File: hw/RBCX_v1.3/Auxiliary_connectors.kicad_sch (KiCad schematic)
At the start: 45 parts

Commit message: Remove stepdowns, Micro-USB; fixup region names
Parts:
- removed X4: (no value), symbol RBCX-eagle-import:614105150621
- D12: value (none) -> SS34; footprint (none) -> RBCX:SMA
- JP32: value (none) -> USB; footprint (none) -> RBCX:1X05
- JP33: value (none) -> SWD; footprint (none) -> RBCX:1X06
- JP34: value (none) -> DEBUG; footprint (none) -> RBCX:1X04
- JP35: value (none) -> USBC_AUX; footprint (none) -> RBCX:1X04
- JP36: value (none) -> BOOT_SW; footprint (none) -> RBCX:1X02
- JP37: value (none) -> ESP32_JTAG; footprint (none) -> RBCX:1X06
- JP38: value (none) -> MPU_I2C; footprint (none) -> RBCX:1X04
- JP39: value (none) -> EXPANDER_UART; footprint (none) -> RBCX:1X06
- JP40: value (none) -> ESP_PROG_UART; footprint (none) -> RBCX:1X04
- JP41: value (none) -> EXPANDER_CAN/I2C; footprint (none) -> RBCX:1X06
- Q9: footprint (none) -> RBCX:SOT23
- R66, R68, R69, R72, R73, R74, R80, R81, R82, R83, R84, R85, R86, R87, R88, R89: value (none) -> 330R; footprint (none) -> RBCX:R0402
- R67: footprint (none) -> RBCX:R0402
- R70: value (none) -> 5k6; footprint (none) -> RBCX:R0402
- R71: value (none) -> 10k; footprint (none) -> RBCX:R0402
- R75: value (none) -> 100k; footprint (none) -> RBCX:R0402
- R76, R77: value (none) -> 5k1; footprint (none) -> RBCX:R0402
- R78, R79: value (none) -> 4k7; footprint (none) -> RBCX:R0402
- SJ6, SJ7: value (none) -> SJ2W0603; footprint (none) -> RBCX:SJ_2_0603
- TP17, TP18, TP19, TP20: value (none) -> TP_06MM; footprint (none) -> RBCX:TP_06
- X3: value (none) -> 52559-3092; footprint (none) -> RBCX:52559-3092
- X5: value (none) -> USB_C_8PIN; footprint (none) -> RBCX:USB_C_VERT_THT_8PIN
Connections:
- net USB_ID: no longer names the net of JP32.4

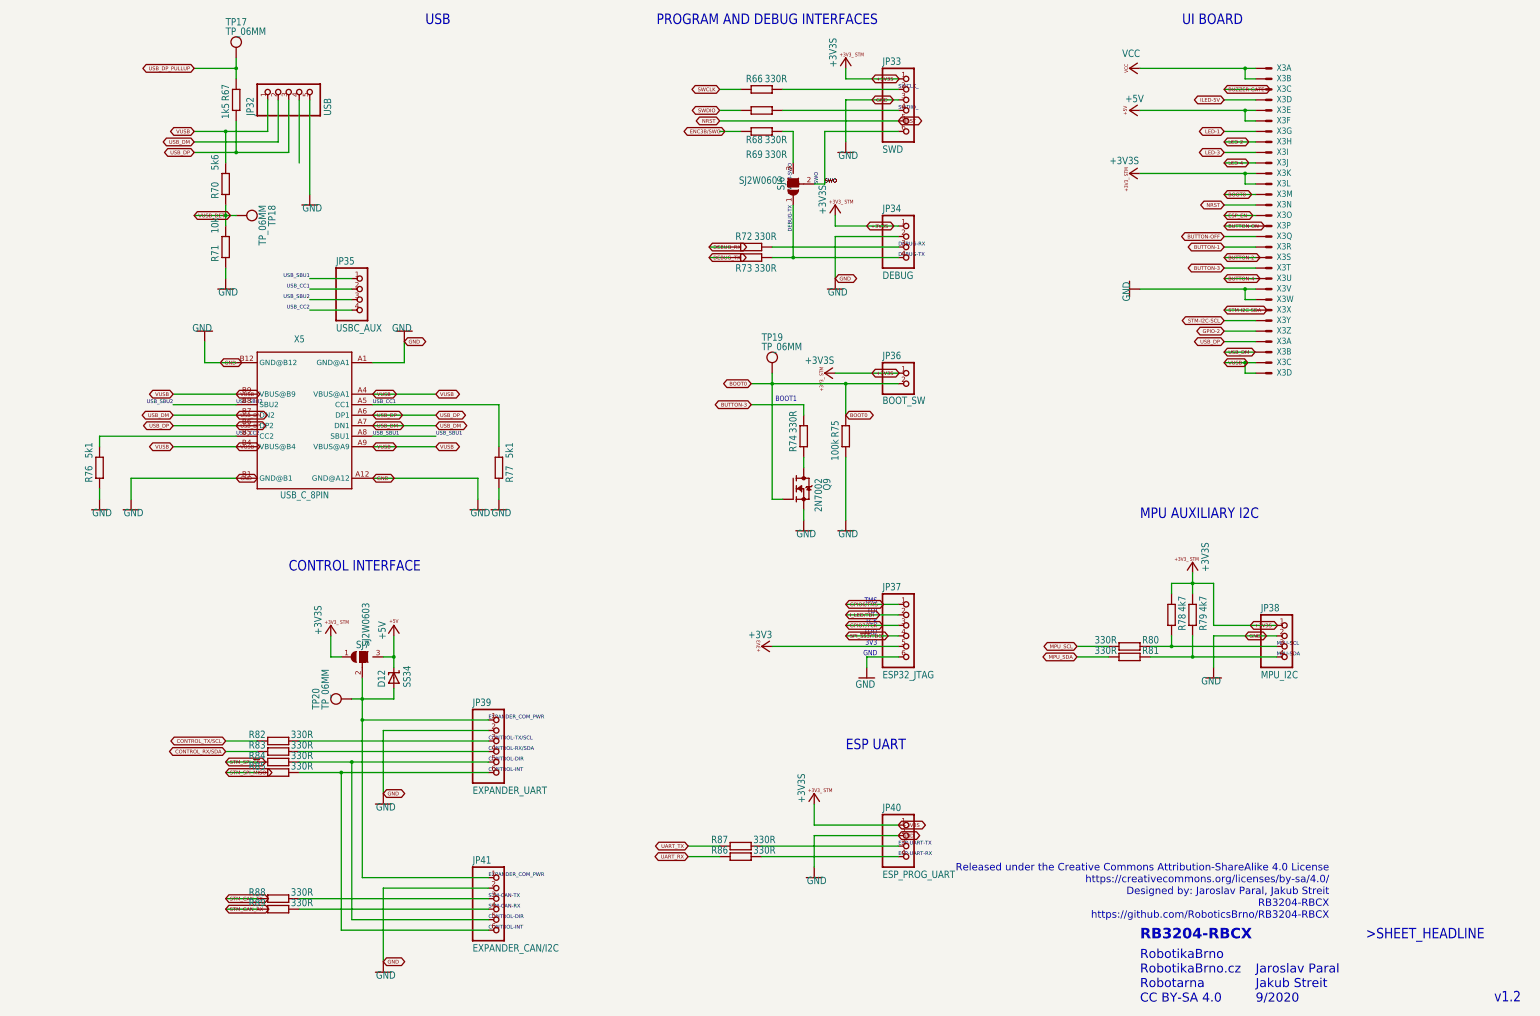
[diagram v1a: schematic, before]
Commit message: Everything everywhere all et once
Conversion to a new look
-  splitting the whole diagram for better orientation on multiple sheets using Kicad functions. Division of the whole schematics within several hierarchical sheets without globally named trac, using only wires, local labels and hierarchical labels.

Add new features
- Battery charger with cell balancer (With whole battery measurement)
- USB PD Sink Controller

Change old features
-  removing many 5V stepdowns and replacing them with only one strong stepdown (continuous 8A, peak 12A)
-  New power switcher design to connect VUSB to the VCC power line when no battery is connected.
(The reason for the new design is the implementation of Power deliveri => high voltage capability on VUSB 5-12V).

Remove micro_USB
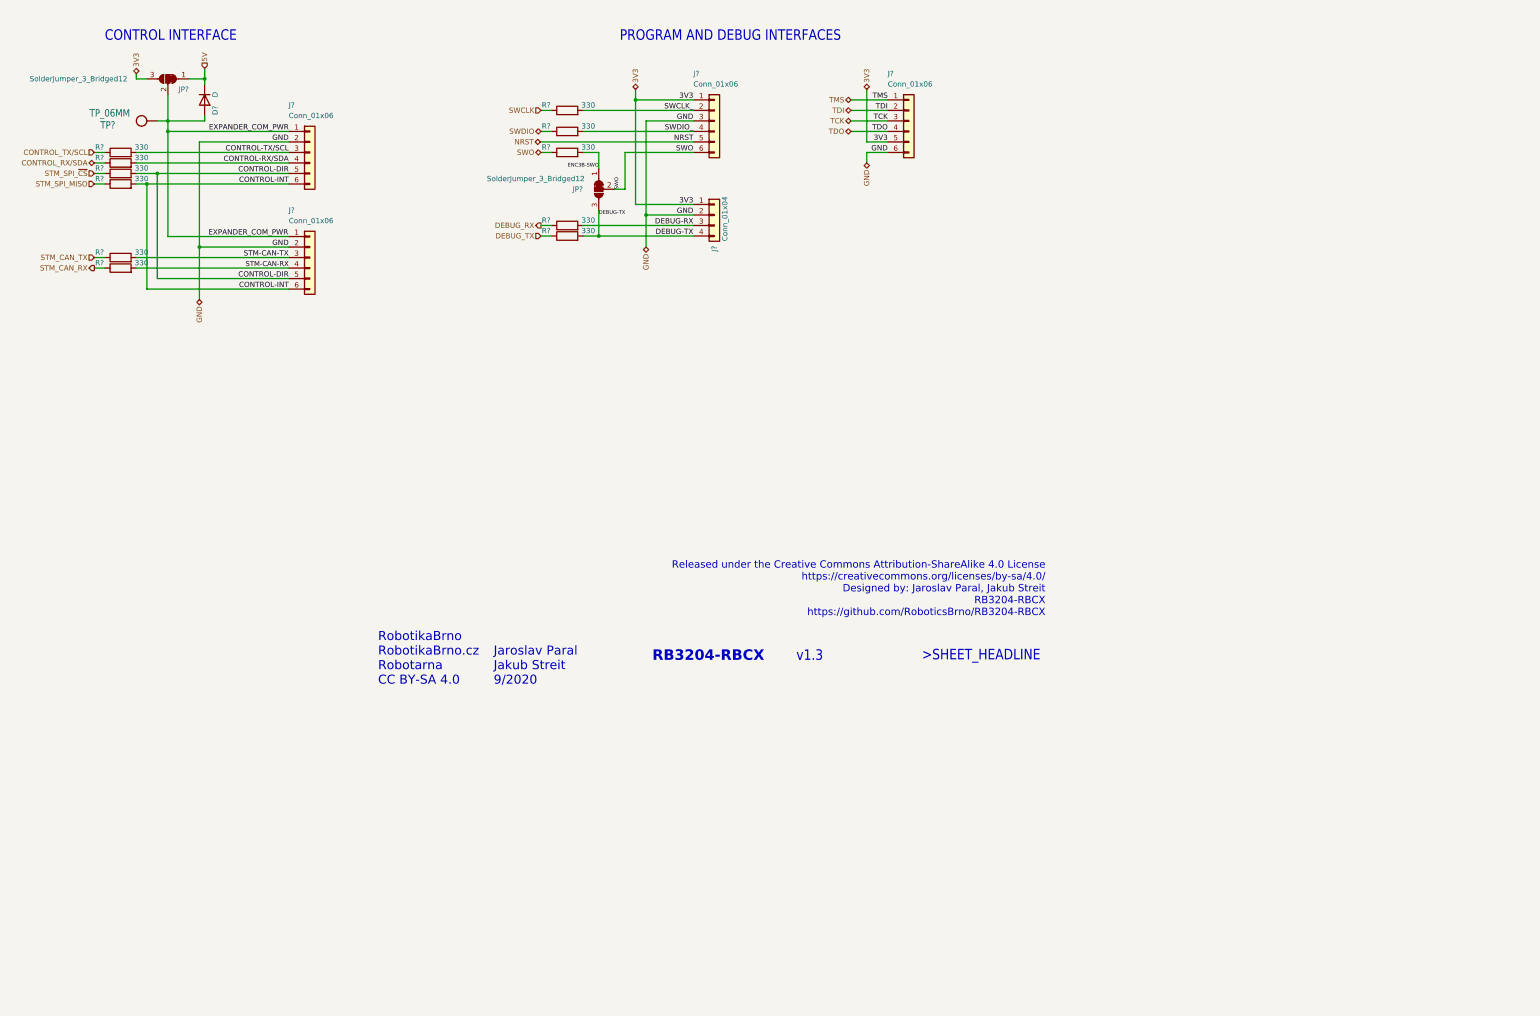
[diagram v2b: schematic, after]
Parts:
- removed D12: SS34, RBCX:SMA, symbol RBCX-eagle-import:SHOTTKY-SMA
- removed JP32: USB, RBCX:1X05, symbol RBCX-eagle-import:PINHD-1X5
- removed JP33: SWD, RBCX:1X06, symbol RBCX-eagle-import:PINHD-1X6
- removed JP34: DEBUG, RBCX:1X04, symbol RBCX-eagle-import:PINHD-1X4
- removed JP35: USBC_AUX, RBCX:1X04, symbol RBCX-eagle-import:PINHD-1X4
- removed JP36: BOOT_SW, RBCX:1X02, symbol RBCX-eagle-import:PINHD-1X2
- removed JP37: ESP32_JTAG, RBCX:1X06, symbol RBCX-eagle-import:PINHD-1X6
- removed JP38: MPU_I2C, RBCX:1X04, symbol RBCX-eagle-import:PINHD-1X4
- removed JP39: EXPANDER_UART, RBCX:1X06, symbol RBCX-eagle-import:PINHD-1X6
- removed JP40: ESP_PROG_UART, RBCX:1X04, symbol RBCX-eagle-import:PINHD-1X4
- removed JP41: EXPANDER_CAN/I2C, RBCX:1X06, symbol RBCX-eagle-import:PINHD-1X6
- removed Q9: (no value), RBCX:SOT23, symbol RBCX-eagle-import:N-MOSFET-SOT23-GSD
- removed R66, R68, R69, R72, R73, R74, R80, R81, R82, R83, R84, R85, R86, R87, R88, R89: 330R, RBCX:R0402, symbol RBCX-eagle-import:R-EU_R0402
- removed R67: (no value), RBCX:R0402, symbol RBCX-eagle-import:R-EU_R0402
- removed R70: 5k6, RBCX:R0402, symbol RBCX-eagle-import:R-EU_R0402
- removed R71: 10k, RBCX:R0402, symbol RBCX-eagle-import:R-EU_R0402
- removed R75: 100k, RBCX:R0402, symbol RBCX-eagle-import:R-EU_R0402
- removed R76, R77: 5k1, RBCX:R0402, symbol RBCX-eagle-import:R-EU_R0402
- removed R78, R79: 4k7, RBCX:R0402, symbol RBCX-eagle-import:R-EU_R0402
- removed SJ6, SJ7: SJ2W0603, RBCX:SJ_2_0603, symbol RBCX-eagle-import:SJ2W0603
- removed TP17, TP18, TP19, TP20: TP_06MM, RBCX:TP_06, symbol RBCX-eagle-import:TP_06MM
- removed X3: 52559-3092, RBCX:52559-3092, symbol RBCX-eagle-import:52559-3092
- removed X5: USB_C_8PIN, RBCX:USB_C_VERT_THT_8PIN, symbol RBCX-eagle-import:USB_C_8PIN
- added D?: D, Diode_SMD:D_SOD-523, symbol Device:D
- added J? (x4): Conn_01x06, Connector_PinHeader_2.54mm:PinHeader_1x06_P2.54mm_Vertical, symbol Connector_Generic:Conn_01x06
- added J?: Conn_01x04, Connector_PinHeader_2.54mm:PinHeader_1x04_P2.54mm_Vertical, symbol Connector_Generic:Conn_01x04
- added JP? (x2): SolderJumper_3_Bridged12, Jumper:SolderJumper-3_P1.3mm_Bridged12_RoundedPad1.0x1.5mm, symbol Jumper:SolderJumper_3_Bridged12
- added R? (x11): 330, Capacitor_SMD:C_0201_0603Metric, symbol Device:R
- added TP?: TP_06MM, RBCX:TP_06MM, symbol RBCX-eagle-import:TP_06MM
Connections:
- net CONTROL-DIR: now also J?.5 (Pin_5), J?.5 (Pin_5), R?.2
- net CONTROL-INT: now also J?.6 (Pin_6), J?.6 (Pin_6), R?.2
- net DEBUG-RX: now also J?.3 (Pin_3), R?.2
- net DEBUG-TX: now also J?.4 (Pin_4), JP?.3 (B), R?.2
- net DEBUG_RX: now also R?.1
- net DEBUG_TX: now also R?.1
- net ENC3B-SWO: now also JP?.1 (A), R?.2
- net EXPANDER_COM_PWR: now also D?.2 (A), J?.1 (Pin_1), J?.1 (Pin_1), JP?.2 (C), TP?.P$1 (TP)
- net GND: now also J?.2 (Pin_2), J?.2 (Pin_2), J?.2 (Pin_2), J?.3 (Pin_3), J?.6 (Pin_6)
- net NRST: now also J?.5 (Pin_5)
- net STM-CAN-RX: now also J?.4 (Pin_4), R?.2
- net STM-CAN-TX: now also J?.3 (Pin_3), R?.2
- net STM_CAN_RX: now also R?.1
- net STM_CAN_TX: now also R?.1
- net STM_SPI_MISO: now also R?.1
- net STM_SPI_~{CS}: now also R?.1
- net SWCLK: now also R?.1
- net SWCLK_: now also J?.2 (Pin_2), R?.2
- net SWDIO: now also R?.1
- net SWDIO_: now also J?.4 (Pin_4), R?.2
- net SWO: now also J?.6 (Pin_6), JP?.2 (C), R?.1
- new net 3V3: J?.1 (Pin_1), J?.1 (Pin_1), J?.5 (Pin_5), JP?.3 (B)
- new net 5V: D?.1 (K), JP?.1 (A)
- new net CONTROL-RX/SDA: J?.4 (Pin_4), R?.2
- new net CONTROL-TX/SCL: J?.3 (Pin_3), R?.2
- new net CONTROL_RX/SDA: R?.1
- new net CONTROL_TX/SCL: R?.1
- new net TCK: J?.3 (Pin_3)
- new net TDI: J?.2 (Pin_2)
- new net TDO: J?.4 (Pin_4)
- new net TMS: J?.1 (Pin_1)
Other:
- note added: "v1.3"
- note removed: "3V3"
- note removed: "BOOT1"
- note removed: "ESP UART"
- note removed: "GND"
- note removed: "MPU AUXILIARY I2C"
- note removed: "TCK"
- note removed: "TDI"
- note removed: "TDO"
- note removed: "TMS"
- note removed: "UI BOARD"
- note removed: "USB"
- note removed: "v1.2"

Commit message: Work in progress
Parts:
- gave numbers to parts that had none: 20
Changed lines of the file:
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@@
   (symbol (lib_id "Device:R") (at 60.96 73.66 90) (unit 1)
     (in_bom yes) (on_board yes)
-    (property "Reference" "R?" (id 0) (at 55.88 72.39 90))
+    (property "Reference" "R50" (id 0) (at 55.88 72.39 90))
     (property "Value" "330" (id 1) (at 66.04 72.39 90))
     (property "Footprint" "Capacitor_SMD:C_0201_0603Metric" (id 2) (at 60.96 75.438 90)
@@
   (symbol (lib_id "Device:R") (at 60.96 93.98 90) (unit 1)
     (in_bom yes) (on_board yes)
-    (property "Reference" "R?" (id 0) (at 55.88 92.71 90))
+    (property "Reference" "R54" (id 0) (at 55.88 92.71 90))
     (property "Value" "330" (id 1) (at 66.04 92.71 90))
     (property "Footprint" "Capacitor_SMD:C_0201_0603Metric" (id 2) (at 60.96 95.758 90)
@@
   (symbol (lib_id "Device:R") (at 168.91 58.42 90) (unit 1)
     (in_bom yes) (on_board yes)
-    (property "Reference" "R?" (id 0) (at 163.83 57.15 90))
+    (property "Reference" "R45" (id 0) (at 163.83 57.15 90))
     (property "Value" "330" (id 1) (at 173.99 57.15 90))
     (property "Footprint" "Capacitor_SMD:C_0201_0603Metric" (id 2) (at 168.91 60.198 90)
@@
   (symbol (lib_id "Device:R") (at 60.96 71.12 90) (unit 1)
     (in_bom yes) (on_board yes)
-    (property "Reference" "R?" (id 0) (at 55.88 69.85 90))
+    (property "Reference" "R49" (id 0) (at 55.88 69.85 90))
     (property "Value" "330" (id 1) (at 66.04 69.85 90))
     (property "Footprint" "Capacitor_SMD:C_0201_0603Metric" (id 2) (at 60.96 72.898 90)
@@
   (symbol (lib_id "Connector_Generic:Conn_01x06") (at 106.68 68.58 0) (unit 1)
     (in_bom yes) (on_board yes)
-    (property "Reference" "J?" (id 0) (at 101.6 57.15 0)
+    (property "Reference" "J26" (id 0) (at 101.6 57.15 0)
       (effects (font (size 1.27 1.27)) (justify left))
     )
@@
   (symbol (lib_id "Jumper:SolderJumper_3_Bridged12") (at 176.53 77.47 90) (mirror x) (unit 1)
     (in_bom yes) (on_board yes)
-    (property "Reference" "JP?" (id 0) (at 171.45 77.47 90))
+    (property "Reference" "JP6" (id 0) (at 171.45 77.47 90))
     (property "Value" "SolderJumper_3_Bridged12" (id 1) (at 161.29 74.93 90))
     (property "Footprint" "Jumper:SolderJumper-3_P1.3mm_Bridged12_RoundedPad1.0x1.5mm" (id 2) (at 176.53 77.47 0)
@@
   (symbol (lib_id "Device:R") (at 168.91 63.5 90) (unit 1)
     (in_bom yes) (on_board yes)
-    (property "Reference" "R?" (id 0) (at 163.83 62.23 90))
+    (property "Reference" "R46" (id 0) (at 163.83 62.23 90))
     (property "Value" "330" (id 1) (at 173.99 62.23 90))
     (property "Footprint" "Capacitor_SMD:C_0201_0603Metric" (id 2) (at 168.91 65.278 90)
@@
   (symbol (lib_id "Connector_Generic:Conn_01x06") (at 106.68 93.98 0) (unit 1)
     (in_bom yes) (on_board yes)
-    (property "Reference" "J?" (id 0) (at 101.6 82.55 0)
+    (property "Reference" "J28" (id 0) (at 101.6 82.55 0)
       (effects (font (size 1.27 1.27)) (justify left))
     )
@@
   (symbol (lib_id "Device:R") (at 168.91 86.233 90) (unit 1)
     (in_bom yes) (on_board yes)
-    (property "Reference" "R?" (id 0) (at 163.83 84.963 90))
+    (property "Reference" "R52" (id 0) (at 163.83 84.963 90))
     (property "Value" "330" (id 1) (at 173.99 84.963 90))
     (property "Footprint" "Capacitor_SMD:C_0201_0603Metric" (id 2) (at 168.91 88.011 90)
@@
   (symbol (lib_id "Connector_Generic:Conn_01x04") (at 204.47 83.693 0) (unit 1)
     (in_bom yes) (on_board yes)
-    (property "Reference" "J?" (id 0) (at 204.47 92.583 90)
+    (property "Reference" "J27" (id 0) (at 204.47 92.583 90)
       (effects (font (size 1.27 1.27)) (justify left))
     )
@@
   (symbol (lib_id "RBCX-eagle-import:TP_06MM") (at 69.85 60.96 90) (unit 1)
     (in_bom yes) (on_board yes)
-    (property "Reference" "TP?" (id 0) (at 59.69 60.96 90)
+    (property "Reference" "TP10" (id 0) (at 59.69 60.96 90)
       (effects (font (size 1.778 1.5113)) (justify left bottom))
     )
@@
   (symbol (lib_id "Device:R") (at 60.96 68.58 90) (unit 1)
     (in_bom yes) (on_board yes)
-    (property "Reference" "R?" (id 0) (at 55.88 67.31 90))
+    (property "Reference" "R47" (id 0) (at 55.88 67.31 90))
     (property "Value" "330" (id 1) (at 66.04 67.31 90))
     (property "Footprint" "Capacitor_SMD:C_0201_0603Metric" (id 2) (at 60.96 70.358 90)
@@
   (symbol (lib_id "Connector_Generic:Conn_01x06") (at 204.47 60.96 0) (unit 1)
     (in_bom yes) (on_board yes)
-    (property "Reference" "J?" (id 0) (at 199.39 49.53 0)
+    (property "Reference" "J24" (id 0) (at 199.39 49.53 0)
       (effects (font (size 1.27 1.27)) (justify left))
     )
@@
   (symbol (lib_id "Device:D") (at 81.28 55.88 270) (unit 1)
     (in_bom yes) (on_board yes)
-    (property "Reference" "D?" (id 0) (at 83.82 58.42 0))
+    (property "Reference" "D2" (id 0) (at 83.82 58.42 0))
     (property "Value" "D" (id 1) (at 83.82 54.61 0))
     (property "Footprint" "Diode_SMD:D_SOD-523" (id 2) (at 81.28 55.88 0)
@@
   (symbol (lib_id "Device:R") (at 60.96 96.52 90) (unit 1)
     (in_bom yes) (on_board yes)
-    (property "Reference" "R?" (id 0) (at 55.88 95.25 90))
+    (property "Reference" "R55" (id 0) (at 55.88 95.25 90))
     (property "Value" "330" (id 1) (at 66.04 95.25 90))
     (property "Footprint" "Capacitor_SMD:C_0201_0603Metric" (id 2) (at 60.96 98.298 90)
@@
   (symbol (lib_id "Device:R") (at 60.96 76.2 90) (unit 1)
     (in_bom yes) (on_board yes)
-    (property "Reference" "R?" (id 0) (at 55.88 74.93 90))
+    (property "Reference" "R51" (id 0) (at 55.88 74.93 90))
     (property "Value" "330" (id 1) (at 66.04 74.93 90))
     (property "Footprint" "Capacitor_SMD:C_0201_0603Metric" (id 2) (at 60.96 77.978 90)
@@
   (symbol (lib_id "Device:R") (at 168.91 88.773 90) (unit 1)
     (in_bom yes) (on_board yes)
-    (property "Reference" "R?" (id 0) (at 163.83 87.503 90))
+    (property "Reference" "R53" (id 0) (at 163.83 87.503 90))
     (property "Value" "330" (id 1) (at 173.99 87.503 90))
     (property "Footprint" "Capacitor_SMD:C_0201_0603Metric" (id 2) (at 168.91 90.551 90)
@@
   (symbol (lib_id "Device:R") (at 168.91 68.58 90) (unit 1)
     (in_bom yes) (on_board yes)
-    (property "Reference" "R?" (id 0) (at 163.83 67.31 90))
+    (property "Reference" "R48" (id 0) (at 163.83 67.31 90))
     (property "Value" "330" (id 1) (at 173.99 67.31 90))
     (property "Footprint" "Capacitor_SMD:C_0201_0603Metric" (id 2) (at 168.91 70.358 90)
@@
   (symbol (lib_id "Jumper:SolderJumper_3_Bridged12") (at 72.39 50.8 0) (mirror y) (unit 1)
     (in_bom yes) (on_board yes)
-    (property "Reference" "JP?" (id 0) (at 76.2 53.34 0))
+    (property "Reference" "JP5" (id 0) (at 76.2 53.34 0))
     (property "Value" "SolderJumper_3_Bridged12" (id 1) (at 50.8 50.8 0))
     (property "Footprint" "Jumper:SolderJumper-3_P1.3mm_Bridged12_RoundedPad1.0x1.5mm" (id 2) (at 72.39 50.8 0)
@@
   (symbol (lib_id "Connector_Generic:Conn_01x06") (at 251.46 60.96 0) (unit 1)
     (in_bom yes) (on_board yes)
-    (property "Reference" "J?" (id 0) (at 246.38 49.53 0)
-      (effects (font (size 1.27 1.27)) (justify left))
-    )
+    (property "Reference" "J25" (id 0) (at 246.38 49.53 0)
+      (effects (font (size 1.27 1.27)) (justify left))
+    )

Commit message: New PCB layout
some changes of schema:
- change PD sink AO33772 to AO33771
- remove power switch
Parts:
- J24, J25, J26, J28: footprint Connector_PinHeader_2.54mm:PinHeader_1x06_P2.54mm_Vertical -> RBCX:PinHeader_1x06_P2.54mm_Vertical
- J27: footprint Connector_PinHeader_2.54mm:PinHeader_1x04_P2.54mm_Vertical -> RBCX:PinHeader_1x04_P2.54mm_Vertical
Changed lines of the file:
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@@
       (effects (font (size 1.27 1.27)) (justify left))
     )
-    (property "Footprint" "Connector_PinHeader_2.54mm:PinHeader_1x06_P2.54mm_Vertical" (id 2) (at 106.68 68.58 0)
+    (property "Footprint" "RBCX:PinHeader_1x06_P2.54mm_Vertical" (id 2) (at 106.68 68.58 0)
       (effects (font (size 1.27 1.27)) hide)
     )
@@
       (effects (font (size 1.27 1.27)) (justify left))
     )
-    (property "Footprint" "Connector_PinHeader_2.54mm:PinHeader_1x06_P2.54mm_Vertical" (id 2) (at 106.68 93.98 0)
+    (property "Footprint" "RBCX:PinHeader_1x06_P2.54mm_Vertical" (id 2) (at 106.68 93.98 0)
       (effects (font (size 1.27 1.27)) hide)
     )
@@
       (effects (font (size 1.27 1.27)) (justify left))
     )
-    (property "Footprint" "Connector_PinHeader_2.54mm:PinHeader_1x04_P2.54mm_Vertical" (id 2) (at 204.47 83.693 0)
+    (property "Footprint" "RBCX:PinHeader_1x04_P2.54mm_Vertical" (id 2) (at 204.47 83.693 0)
       (effects (font (size 1.27 1.27)) hide)
     )
@@
       (effects (font (size 1.27 1.27)) (justify left))
     )
-    (property "Footprint" "Connector_PinHeader_2.54mm:PinHeader_1x06_P2.54mm_Vertical" (id 2) (at 204.47 60.96 0)
+    (property "Footprint" "RBCX:PinHeader_1x06_P2.54mm_Vertical" (id 2) (at 204.47 60.96 0)
       (effects (font (size 1.27 1.27)) hide)
     )
@@
       (effects (font (size 1.27 1.27)) (justify left))
     )
-    (property "Footprint" "Connector_PinHeader_2.54mm:PinHeader_1x06_P2.54mm_Vertical" (id 2) (at 251.46 60.96 0)
-      (effects (font (size 1.27 1.27)) hide)
-    )
+    (property "Footprint" "RBCX:PinHeader_1x06_P2.54mm_Vertical" (id 2) (at 251.46 60.96 0)
+      (effects (font (size 1.27 1.27)) hide)
+    )
